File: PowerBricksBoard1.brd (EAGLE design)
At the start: 160 x 100 mm, 15 parts

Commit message: layout
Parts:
- removed U$2: PMBUSTABLE, PMBUS Resistors:0603
- added R3: (no value), SparkFun-Resistors:0603
- moved H4 169.9 mm to (72.4, 3.81), turned to 90 degrees
- moved H2 142.0 mm to (72.4, 47.0), turned to 90 degrees
- moved R4 120.5 mm to (69.8, 25.4), turned to 90 degrees
- moved H3 109.6 mm to (3.81, 3.81), turned to 90 degrees
- moved C3 106.0 mm to (29.2, 14.0), turned to 180 degrees
- moved D1 105.2 mm to (58.4, 40.6), turned to 180 degrees
- moved R1 99.4 mm to (62.2, 40.6)
- moved D2 90.5 mm to (38.1, 41.9), turned to 180 degrees
- moved U$1 90.4 mm to (12.7, 16.5)
- moved R2 85.5 mm to (39.4, 38.1), turned to 90 degrees
- moved C2 80.5 mm to (29.2, 36.8), turned to 180 degrees
- moved C1 78.5 mm to (29.2, 25.4), turned to 180 degrees
- moved U$6 76.2 mm to (17.8, 40.6), turned to 270 degrees
- moved H1 72.3 mm to (3.81, 47.0), turned to 90 degrees
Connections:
- net DGND: now also R3.1; no longer U$2.1
- net N$3: now also R3.2; no longer U$2.2
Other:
- board size 160 x 100 mm -> 76.2 x 50.8 mm

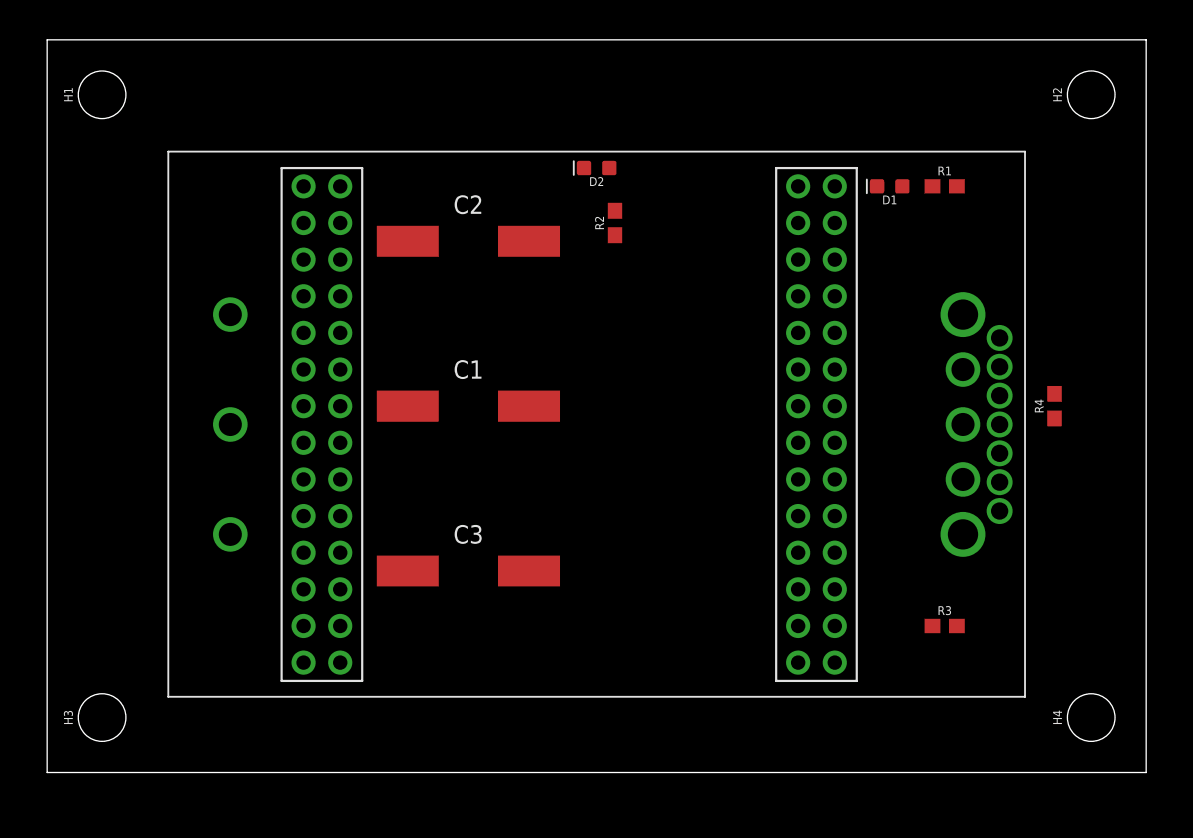
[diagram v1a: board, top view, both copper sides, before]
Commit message: power plane polygons routed, board layout set. Schematic and IO work remains as well as the octa table
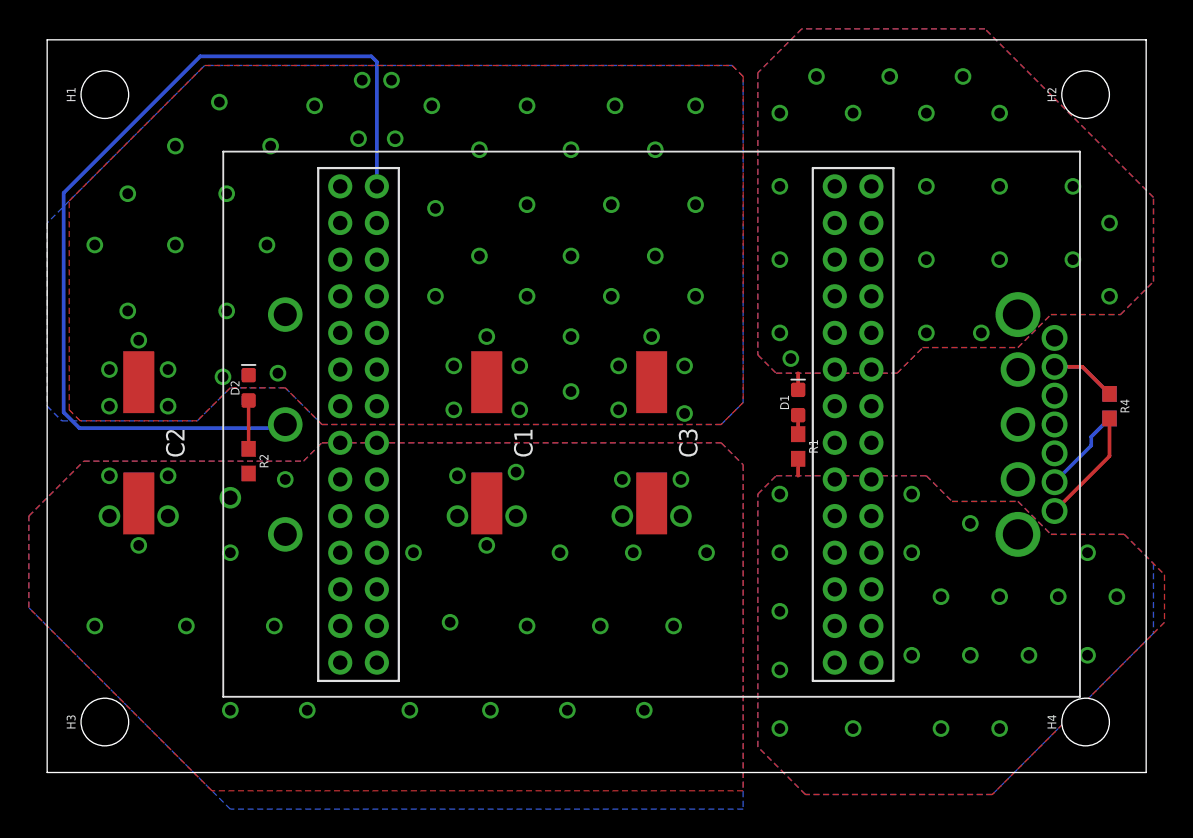
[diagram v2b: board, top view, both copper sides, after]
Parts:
- moved R2 30.3 mm to (14.0, 21.6), turned to 270 degrees
- moved D2 28.5 mm to (14.0, 26.7), turned to 90 degrees
- moved C2 26.8 mm to (6.35, 22.9), turned to 90 degrees
- moved R1 20.7 mm to (52.1, 22.6), turned to 270 degrees
- moved R3 19.0 mm to (73.7, 25.4), flipped to the bottom, turned to 270 degrees
- moved D1 16.3 mm to (52.1, 25.7), turned to 90 degrees
- moved C3 15.5 mm to (41.9, 22.9), turned to 90 degrees
- moved R4 3.81 mm to (73.7, 25.4), turned to 270 degrees
- moved U$1 3.81 mm to (16.5, 16.5)
- moved C1 2.84 mm to (30.5, 22.9), turned to 90 degrees
- moved U$6 2.54 mm to (20.3, 40.6)
- moved H4 0.50 mm to (72.0, 3.50)
- moved H2 0.39 mm to (72.0, 47.0)
- moved H3 0.36 mm to (4.00, 3.50)
- moved H1 0.19 mm to (4.00, 47.0)
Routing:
- net ON/OFF: track 0.00 -> 65.6 mm
- net DGND: track 0.00 -> 9.18 mm
- net N$4: track 0.00 -> 8.00 mm
- net N$3: track 0.00 -> 6.00 mm
- net N$2: track 0.00 -> 3.35 mm
- net N$1: track 0.00 -> 1.32 mm
- net 12V: track 0.00 -> 1.18 mm, vias 0 -> 20
- net 12_GND: track 0.00 -> 1.16 mm, vias 0 -> 21
- added copper zone on layer 1, net 12V
- added copper zone on layer 16, net 12V
- added copper zone on layer 1, net 12_GND
- added copper zone on layer 16, net 12_GND
- added copper zone on layer 1, net 48V
- added copper zone on layer 16, net 48V
- added copper zone on layer 1, net 48_GND
- added copper zone on layer 16, net 48_GND

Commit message: planes: good
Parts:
- moved R2 1.27 mm to (13.7, 22.8)
- moved D2 0.90 mm to (13.7, 25.8)
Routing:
- net N$2: track 3.35 -> 1.24 mm
- net ON/OFF: track 65.6 -> 67.3 mm
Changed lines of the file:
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@@
 <setting verticaltext="up"/>
 </settings>
-<grid distance="10" unitdist="mil" unit="mil" style="lines" multiple="1" display="no" altdistance="5" altunitdist="mil" altunit="mil"/>
+<grid distance="2" unitdist="mil" unit="mil" style="lines" multiple="1" display="no" altdistance="5" altunitdist="mil" altunit="mil"/>
 <layers>
 <layer number="1" name="Top" color="4" fill="1" visible="yes" active="yes"/>
@@
 <attribute name="VALUE" x="52.705" y="25.654" size="0.6096" layer="27" font="vector" ratio="20" rot="R90" align="top-center"/>
 </element>
-<element name="D2" library="SparkFun-LED" library_urn="urn:adsk.eagle:library:529" package="LED-0603" package3d_urn="urn:adsk.eagle:package:39354/1" value="" x="13.97" y="26.67" smashed="yes" rot="R90">
-<attribute name="NAME" x="13.335" y="26.67" size="0.6096" layer="25" font="vector" ratio="20" rot="R90" align="bottom-center"/>
-<attribute name="VALUE" x="14.605" y="26.67" size="0.6096" layer="27" font="vector" ratio="20" rot="R90" align="top-center"/>
+<element name="D2" library="SparkFun-LED" library_urn="urn:adsk.eagle:library:529" package="LED-0603" package3d_urn="urn:adsk.eagle:package:39354/1" value="" x="13.716" y="25.8064" smashed="yes" rot="R90">
+<attribute name="NAME" x="13.081" y="25.8064" size="0.6096" layer="25" font="vector" ratio="20" rot="R90" align="bottom-center"/>
+<attribute name="VALUE" x="14.351" y="25.8064" size="0.6096" layer="27" font="vector" ratio="20" rot="R90" align="top-center"/>
 </element>
 <element name="H1" library="SparkFun-Hardware" library_urn="urn:adsk.eagle:library:519" package="STAND-OFF" package3d_urn="urn:adsk.eagle:package:38630/1" value="STAND-OFF" x="4" y="47" smashed="yes" rot="R90">
@@
 <attribute name="VALUE" x="51.308" y="22.606" size="0.6096" layer="27" font="vector" ratio="20" rot="R270" align="top-center"/>
 </element>
-<element name="R2" library="SparkFun-Resistors" library_urn="urn:adsk.eagle:library:532" package="0603" package3d_urn="urn:adsk.eagle:package:39650/1" value="470" x="13.97" y="21.59" smashed="yes" rot="R270">
-<attribute name="NAME" x="14.732" y="21.59" size="0.6096" layer="25" font="vector" ratio="20" rot="R270" align="bottom-center"/>
-<attribute name="PROD_ID" value=" " x="-80.01" y="-3.81" size="1.778" layer="27" rot="R270" display="off"/>
-<attribute name="VALUE" x="13.208" y="21.59" size="0.6096" layer="27" font="vector" ratio="20" rot="R270" align="top-center"/>
+<element name="R2" library="SparkFun-Resistors" library_urn="urn:adsk.eagle:library:532" package="0603" package3d_urn="urn:adsk.eagle:package:39650/1" value="470" x="13.716" y="22.8346" smashed="yes" rot="R270">
+<attribute name="NAME" x="14.478" y="22.8346" size="0.6096" layer="25" font="vector" ratio="20" rot="R270" align="bottom-center"/>
+<attribute name="PROD_ID" value=" " x="-80.264" y="-2.5654" size="1.778" layer="27" rot="R270" display="off"/>
+<attribute name="VALUE" x="12.954" y="22.8346" size="0.6096" layer="27" font="vector" ratio="20" rot="R270" align="top-center"/>
 </element>
 <element name="R4" library="SparkFun-Resistors" library_urn="urn:adsk.eagle:library:532" package="0603" package3d_urn="urn:adsk.eagle:package:39650/1" value=" " x="73.66" y="25.4" smashed="yes" rot="R270">
@@
 <contactref element="R2" pad="2"/>
 <polygon width="0.254" layer="1">
-<vertex x="2.54" y="21.59"/>
-<vertex x="17.78" y="21.59"/>
-<vertex x="19.05" y="22.86"/>
-<vertex x="46.736" y="22.86"/>
-<vertex x="48.26" y="21.336"/>
+<vertex x="1.9304" y="22.4028"/>
+<vertex x="17.3736" y="22.4028"/>
+<vertex x="18.1356" y="23.1648"/>
+<vertex x="47.1424" y="23.1648"/>
+<vertex x="48.26" y="22.0472"/>
 <vertex x="48.26" y="-1.27"/>
 <vertex x="11.43" y="-1.27"/>
 <vertex x="-1.27" y="11.43"/>
-<vertex x="-1.27" y="17.78"/>
+<vertex x="-1.27" y="19.2024"/>
 </polygon>
 <polygon width="0.254" layer="16">
-<vertex x="2.54" y="21.59"/>
-<vertex x="17.78" y="21.59"/>
-<vertex x="19.05" y="22.86"/>
-<vertex x="46.736" y="22.86"/>
-<vertex x="48.26" y="21.336"/>
+<vertex x="1.9558" y="22.4028"/>
+<vertex x="17.3736" y="22.4028"/>
+<vertex x="18.1356" y="23.1648"/>
+<vertex x="47.1424" y="23.1648"/>
+<vertex x="48.26" y="22.0472"/>
 <vertex x="48.26" y="-2.54"/>
 <vertex x="12.7" y="-2.54"/>
 <vertex x="-1.27" y="11.43"/>
-<vertex x="-1.27" y="17.78"/>
+<vertex x="-1.27" y="19.177"/>
 </polygon>
 <via x="28.448" y="17.78" extent="1-16" drill="1"/>
 <via x="32.512" y="17.78" extent="1-16" drill="1"/>
-<via x="12.7" y="19.05" extent="1-16" drill="1"/>
+<via x="12.5984" y="19.6088" extent="1-16" drill="1"/>
 <via x="8.382" y="17.78" extent="1-16" drill="1"/>
 <via x="4.318" y="17.78" extent="1-16" drill="1"/>
@@
 <via x="12.7" y="15.24" extent="1-16" drill="0.75"/>
 <via x="15.748" y="10.16" extent="1-16" drill="0.75"/>
-<via x="16.51" y="20.32" extent="1-16" drill="0.75"/>
+<via x="15.8496" y="21.4376" extent="1-16" drill="0.75"/>
 <via x="45.72" y="15.24" extent="1-16" drill="0.75"/>
 <via x="28.448" y="20.574" extent="1-16" drill="0.75"/>
@@
 <contactref element="D2" pad="C"/>
 <polygon width="0.254" layer="16" isolate="0.254">
-<vertex x="12.7" y="26.67"/>
-<vertex x="16.51" y="26.67"/>
-<vertex x="19.05" y="24.13"/>
-<vertex x="46.736" y="24.13"/>
-<vertex x="48.26" y="25.654"/>
+<vertex x="12.954" y="25.7048"/>
+<vertex x="17.3736" y="25.7048"/>
+<vertex x="18.9484" y="24.13"/>
+<vertex x="46.8884" y="24.13"/>
+<vertex x="48.26" y="25.5016"/>
 <vertex x="48.26" y="48.26"/>
 <vertex x="47.498" y="49.022"/>
 <vertex x="10.922" y="49.022"/>
 <vertex x="0" y="38.1"/>
-<vertex x="0" y="25.4"/>
-<vertex x="1.016" y="24.384"/>
-<vertex x="10.414" y="24.384"/>
+<vertex x="0" y="25.146"/>
+<vertex x="2.1844" y="22.9616"/>
+<vertex x="10.2108" y="22.9616"/>
 </polygon>
 <polygon width="0.254" layer="1">
-<vertex x="48.26" y="25.654"/>
-<vertex x="46.736" y="24.13"/>
-<vertex x="19.05" y="24.13"/>
-<vertex x="16.51" y="26.67"/>
-<vertex x="12.7" y="26.67"/>
-<vertex x="10.414" y="24.384"/>
-<vertex x="2.286" y="24.384"/>
-<vertex x="1.524" y="25.146"/>
-<vertex x="1.524" y="39.624"/>
+<vertex x="48.26" y="25.5016"/>
+<vertex x="46.863" y="24.1046"/>
+<vertex x="18.9738" y="24.1046"/>
+<vertex x="17.3736" y="25.7048"/>
+<vertex x="12.9794" y="25.7048"/>
+<vertex x="10.5918" y="23.3172"/>
+<vertex x="1.9812" y="23.3172"/>
+<vertex x="1.6256" y="23.6728"/>
+<vertex x="1.6256" y="39.7256"/>
 <vertex x="10.922" y="49.022"/>
 <vertex x="47.498" y="49.022"/>
@@
 <via x="36.322" y="43.18" extent="1-16" drill="0.75"/>
 <via x="29.972" y="43.18" extent="1-16" drill="0.75"/>
-<via x="24.13" y="43.942" extent="1-16" drill="0.75"/>
-<via x="23.876" y="48.006" extent="1-16" drill="0.75"/>
-<via x="21.844" y="48.006" extent="1-16" drill="0.75"/>
+<via x="24.2824" y="43.8912" extent="1-16" drill="0.75"/>
+<via x="24.1808" y="48.1584" extent="1-16" drill="0.75"/>
+<via x="21.59" y="48.1584" extent="1-16" drill="0.75"/>
 <via x="21.59" y="43.942" extent="1-16" drill="0.75"/>
 <via x="33.274" y="46.228" extent="1-16" drill="0.75"/>
@@
 <via x="12.192" y="27.432" extent="1-16" drill="0.75"/>
 <via x="16.002" y="27.686" extent="1-16" drill="0.75"/>
+<via x="24.2316" y="45.9232" extent="1-16" drill="0.75"/>
+<via x="21.59" y="46.0248" extent="1-16" drill="0.75"/>
 </signal>
 <signal name="12V">
@@
 <contactref element="U$6" pad="1"/>
 <contactref element="U$1" pad="ON/OFF"/>
-<wire x1="16.51" y1="24.13" x2="16.256" y2="23.876" width="0.254" layer="16"/>
-<wire x1="16.256" y1="23.876" x2="2.2352" y2="23.876" width="0.254" layer="16"/>
-<wire x1="2.2352" y1="23.876" x2="1.143" y2="24.9682" width="0.254" layer="16"/>
-<wire x1="1.143" y1="24.9682" x2="1.143" y2="40.1828" width="0.254" layer="16"/>
+<wire x1="16.51" y1="24.13" x2="15.24" y2="22.86" width="0.254" layer="16"/>
+<wire x1="15.24" y1="22.86" x2="1.7272" y2="22.86" width="0.254" layer="16"/>
+<wire x1="1.7272" y1="22.86" x2="1.143" y2="23.4442" width="0.254" layer="16"/>
+<wire x1="1.143" y1="23.4442" x2="1.143" y2="40.1828" width="0.254" layer="16"/>
 <wire x1="1.143" y1="40.1828" x2="10.6172" y2="49.657" width="0.254" layer="16"/>
 <wire x1="10.6172" y1="49.657" x2="22.479" y2="49.657" width="0.254" layer="16"/>
@@
 <contactref element="R2" pad="1"/>
 <contactref element="D2" pad="A"/>
-<wire x1="13.97" y1="25.793" x2="13.97" y2="22.44" width="0.254" layer="1"/>
+<wire x1="13.716" y1="24.9294" x2="13.716" y2="23.6846" width="0.254" layer="1"/>
 </signal>
 <signal name="DGND">

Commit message: schematic update in 2 days (in valve time)
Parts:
- moved D1 1.63 mm to (50.4, 25.7)
- moved R1 1.63 mm to (50.4, 22.7)
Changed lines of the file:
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@@
 <attribute name="NAME" x="44.45" y="22.86" size="1.27" layer="25" rot="R90" align="center"/>
 </element>
-<element name="D1" library="SparkFun-LED" library_urn="urn:adsk.eagle:library:529" package="LED-0603" package3d_urn="urn:adsk.eagle:package:39354/1" value="" x="52.07" y="25.654" smashed="yes" rot="R90">
-<attribute name="NAME" x="51.435" y="25.654" size="0.6096" layer="25" font="vector" ratio="20" rot="R90" align="bottom-center"/>
-<attribute name="VALUE" x="52.705" y="25.654" size="0.6096" layer="27" font="vector" ratio="20" rot="R90" align="top-center"/>
+<element name="D1" library="SparkFun-LED" library_urn="urn:adsk.eagle:library:529" package="LED-0603" package3d_urn="urn:adsk.eagle:package:39354/1" value="" x="50.4444" y="25.7048" smashed="yes" rot="R90">
+<attribute name="NAME" x="49.8094" y="25.7048" size="0.6096" layer="25" font="vector" ratio="20" rot="R90" align="bottom-center"/>
+<attribute name="VALUE" x="51.0794" y="25.7048" size="0.6096" layer="27" font="vector" ratio="20" rot="R90" align="top-center"/>
 </element>
 <element name="D2" library="SparkFun-LED" library_urn="urn:adsk.eagle:library:529" package="LED-0603" package3d_urn="urn:adsk.eagle:package:39354/1" value="" x="13.716" y="25.8064" smashed="yes" rot="R90">
@@
 <attribute name="VALUE" x="74.032" y="3.5" size="0.6096" layer="27" font="vector" ratio="20" rot="R90" align="top-center"/>
 </element>
-<element name="R1" library="SparkFun-Resistors" library_urn="urn:adsk.eagle:library:532" package="0603" package3d_urn="urn:adsk.eagle:package:39650/1" value="470" x="52.07" y="22.606" smashed="yes" rot="R270">
-<attribute name="NAME" x="52.832" y="22.606" size="0.6096" layer="25" font="vector" ratio="20" rot="R270" align="bottom-center"/>
-<attribute name="PROD_ID" value=" " x="-41.91" y="1.016" size="1.778" layer="27" rot="R270" display="off"/>
-<attribute name="VALUE" x="51.308" y="22.606" size="0.6096" layer="27" font="vector" ratio="20" rot="R270" align="top-center"/>
+<element name="R1" library="SparkFun-Resistors" library_urn="urn:adsk.eagle:library:532" package="0603" package3d_urn="urn:adsk.eagle:package:39650/1" value="470" x="50.4444" y="22.6568" smashed="yes" rot="R270">
+<attribute name="NAME" x="51.2064" y="22.6568" size="0.6096" layer="25" font="vector" ratio="20" rot="R270" align="bottom-center"/>
+<attribute name="PROD_ID" value=" " x="-43.5356" y="1.0668" size="1.778" layer="27" rot="R270" display="off"/>
+<attribute name="VALUE" x="49.6824" y="22.6568" size="0.6096" layer="27" font="vector" ratio="20" rot="R270" align="top-center"/>
 </element>
 <element name="R2" library="SparkFun-Resistors" library_urn="urn:adsk.eagle:library:532" package="0603" package3d_urn="urn:adsk.eagle:package:39650/1" value="470" x="13.716" y="22.8346" smashed="yes" rot="R270">
@@
 <polygon width="0.254" layer="1">
 <vertex x="1.9304" y="22.4028"/>
-<vertex x="17.3736" y="22.4028"/>
-<vertex x="18.1356" y="23.1648"/>
-<vertex x="47.1424" y="23.1648"/>
+<vertex x="17.6276" y="22.4028"/>
+<vertex x="18.1356" y="22.9108"/>
+<vertex x="47.3964" y="22.9108"/>
 <vertex x="48.26" y="22.0472"/>
 <vertex x="48.26" y="-1.27"/>
@@
 <polygon width="0.254" layer="16">
 <vertex x="1.9558" y="22.4028"/>
-<vertex x="17.3736" y="22.4028"/>
-<vertex x="18.1356" y="23.1648"/>
-<vertex x="47.1424" y="23.1648"/>
+<vertex x="17.6276" y="22.4028"/>
+<vertex x="18.1356" y="22.9108"/>
+<vertex x="47.3964" y="22.9108"/>
 <vertex x="48.26" y="22.0472"/>
 <vertex x="48.26" y="-2.54"/>
@@
 <vertex x="17.3736" y="25.7048"/>
 <vertex x="12.9794" y="25.7048"/>
-<vertex x="10.5918" y="23.3172"/>
-<vertex x="1.9812" y="23.3172"/>
+<vertex x="10.6934" y="23.4188"/>
+<vertex x="1.8796" y="23.4188"/>
 <vertex x="1.6256" y="23.6728"/>
 <vertex x="1.6256" y="39.7256"/>
@@
 <via x="36.322" y="43.18" extent="1-16" drill="0.75"/>
 <via x="29.972" y="43.18" extent="1-16" drill="0.75"/>
-<via x="24.2824" y="43.8912" extent="1-16" drill="0.75"/>
-<via x="24.1808" y="48.1584" extent="1-16" drill="0.75"/>
-<via x="21.59" y="48.1584" extent="1-16" drill="0.75"/>
-<via x="21.59" y="43.942" extent="1-16" drill="0.75"/>
+<via x="24.2316" y="43.18" extent="1-16" drill="0.75"/>
+<via x="24.1808" y="47.498" extent="1-16" drill="0.75"/>
+<via x="21.6916" y="47.4472" extent="1-16" drill="0.75"/>
+<via x="21.7424" y="43.18" extent="1-16" drill="0.75"/>
 <via x="33.274" y="46.228" extent="1-16" drill="0.75"/>
 <via x="39.37" y="46.228" extent="1-16" drill="0.75"/>
@@
 <via x="26.67" y="46.228" extent="1-16" drill="0.75"/>
 <via x="11.938" y="46.482" extent="1-16" drill="0.75"/>
-<via x="18.542" y="46.228" extent="1-16" drill="0.75"/>
+<via x="18.3388" y="46.1772" extent="1-16" drill="0.75"/>
 <via x="8.89" y="43.434" extent="1-16" drill="0.75"/>
 <via x="3.302" y="36.576" extent="1-16" drill="0.75"/>
@@
 <via x="12.192" y="27.432" extent="1-16" drill="0.75"/>
 <via x="16.002" y="27.686" extent="1-16" drill="0.75"/>
-<via x="24.2316" y="45.9232" extent="1-16" drill="0.75"/>
-<via x="21.59" y="46.0248" extent="1-16" drill="0.75"/>
+<via x="24.1808" y="45.212" extent="1-16" drill="0.75"/>
+<via x="21.6916" y="45.212" extent="1-16" drill="0.75"/>
 </signal>
 <signal name="12V">
@@
 <vertex x="50.546" y="20.574"/>
 </polygon>
-<wire x1="52.07" y1="21.756" x2="52.07" y2="20.574" width="0.254" layer="1"/>
+<wire x1="50.4444" y1="21.8068" x2="50.4444" y2="20.32" width="0.254" layer="1"/>
 <via x="59.944" y="19.304" extent="1-16" drill="0.75"/>
 <via x="64.008" y="17.272" extent="1-16" drill="0.75"/>
@@
 <vertex x="49.276" y="28.956"/>
 </polygon>
-<wire x1="52.07" y1="26.531" x2="52.07" y2="27.686" width="0.254" layer="1"/>
+<wire x1="50.4444" y1="26.5818" x2="50.4444" y2="28.0416" width="0.254" layer="1"/>
 <via x="51.562" y="28.702" extent="1-16" drill="0.75"/>
 <via x="50.8" y="30.48" extent="1-16" drill="0.75"/>
@@
 <contactref element="R1" pad="1"/>
 <contactref element="D1" pad="A"/>
-<wire x1="52.07" y1="24.777" x2="52.07" y2="23.456" width="0.254" layer="1"/>
+<wire x1="50.4444" y1="24.8278" x2="50.4444" y2="23.5068" width="0.254" layer="1"/>
 </signal>
 <signal name="N$2">

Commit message: owo
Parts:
- moved D1 0.25 mm to (50.2, 25.7)
- moved R1 0.25 mm to (50.2, 22.7)
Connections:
- net 12V: now also U$1.SENSE+
- net 12_GND: now also U$1.SENSE-
- net ON/OFF: now also U$1.C2
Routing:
- net ON/OFF: track 67.3 -> 137.9 mm
- net CLK: track 0.00 -> 16.1 mm
- net DATA: track 0.00 -> 15.9 mm
- net ALERT: track 0.00 -> 13.7 mm
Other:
- board text added: "ADDR1 = R3 Resistor ADDR0 = R4 Resistor Octal Address = 8*ADDR1 + ADDR0"
- board text added: "Octal digit -> Resistor(Kohm) _________ 0 | 10 1 | 15.4 2 | 23.7 3 | 36.5 4 | 54.9 5 | 84.5 6 | 130 7 | 200"
